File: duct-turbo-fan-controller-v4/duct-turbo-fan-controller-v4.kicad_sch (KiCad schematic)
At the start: 45 parts, among them J1 Screw_Terminal_01x04, J2 Conn_01x04, J3 USB_OTG, J4 AudioJack4, J7 Conn_01x04, Q1 MMBT3904, Q2 BSS84, SW1 SW_Push, SW2 SW_Push, U1 SCD41-D-R2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

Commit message: Reduce size of R8 to 0603. Improve labels of LEDs.
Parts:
- R8: footprint Resistor_SMD:R_0805_2012Metric_Pad1.20x1.40mm_HandSolder -> Resistor_SMD:R_0603_1608Metric_Pad0.98x0.95mm_HandSolder
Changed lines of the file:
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@@
 			)
 		)
-		(property "Footprint" "Resistor_SMD:R_0805_2012Metric_Pad1.20x1.40mm_HandSolder"
+		(property "Footprint" "Resistor_SMD:R_0603_1608Metric_Pad0.98x0.95mm_HandSolder"
 			(at 96.52 77.47 0)
 			(effects

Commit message: Add values to led resistors. Redraw zone fills.
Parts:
- D4: value LED_Small -> LED Green
- D5: value LED_Small -> LED Red
- R15, R16: value R_Small -> 1k
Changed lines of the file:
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@@
 			)
 		)
-		(property "Value" "R_Small"
+		(property "Value" "1k"
 			(at 243.84 27.9399 0)
 			(effects
@@
 			)
 		)
-		(property "Value" "LED_Small"
+		(property "Value" "LED Green"
 			(at 259.08 32.9564 90)
 			(effects
@@
 			)
 		)
-		(property "Value" "R_Small"
+		(property "Value" "1k"
 			(at 259.08 27.9399 0)
 			(effects
@@
 			)
 		)
-		(property "Value" "LED_Small"
+		(property "Value" "LED Red"
 			(at 243.84 32.9564 90)
 			(effects

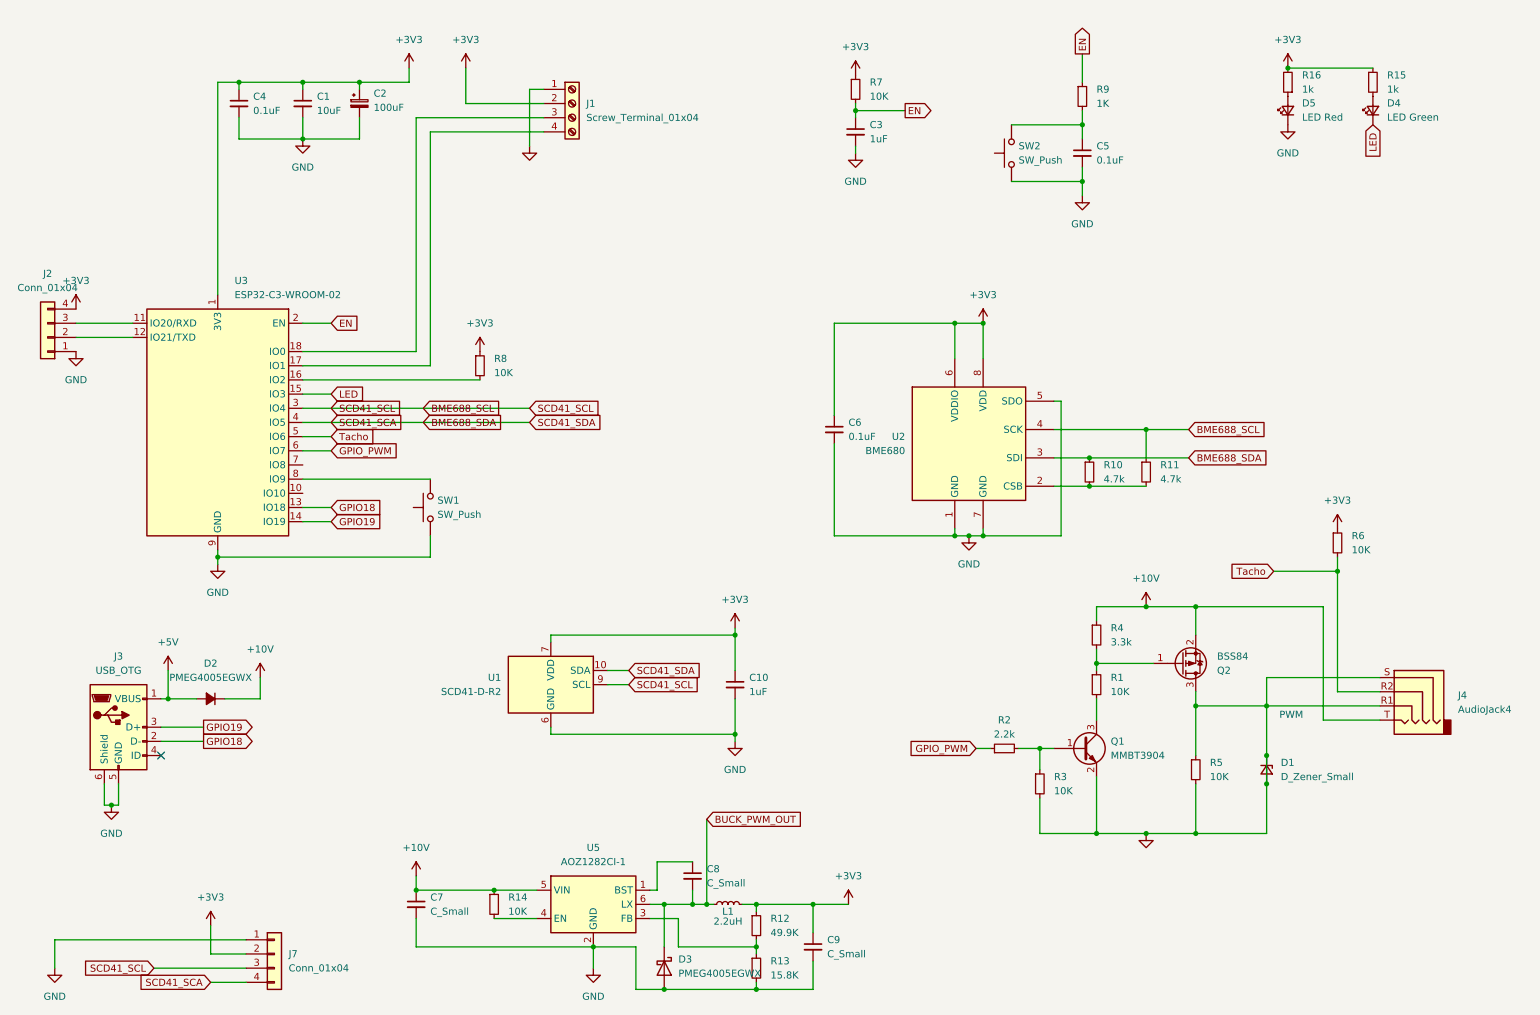
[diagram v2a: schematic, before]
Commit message: Fix a couple of schematic errors.
1. External PWM was tied to ground.
2. BME688 SCA and SCL pins were tied together.
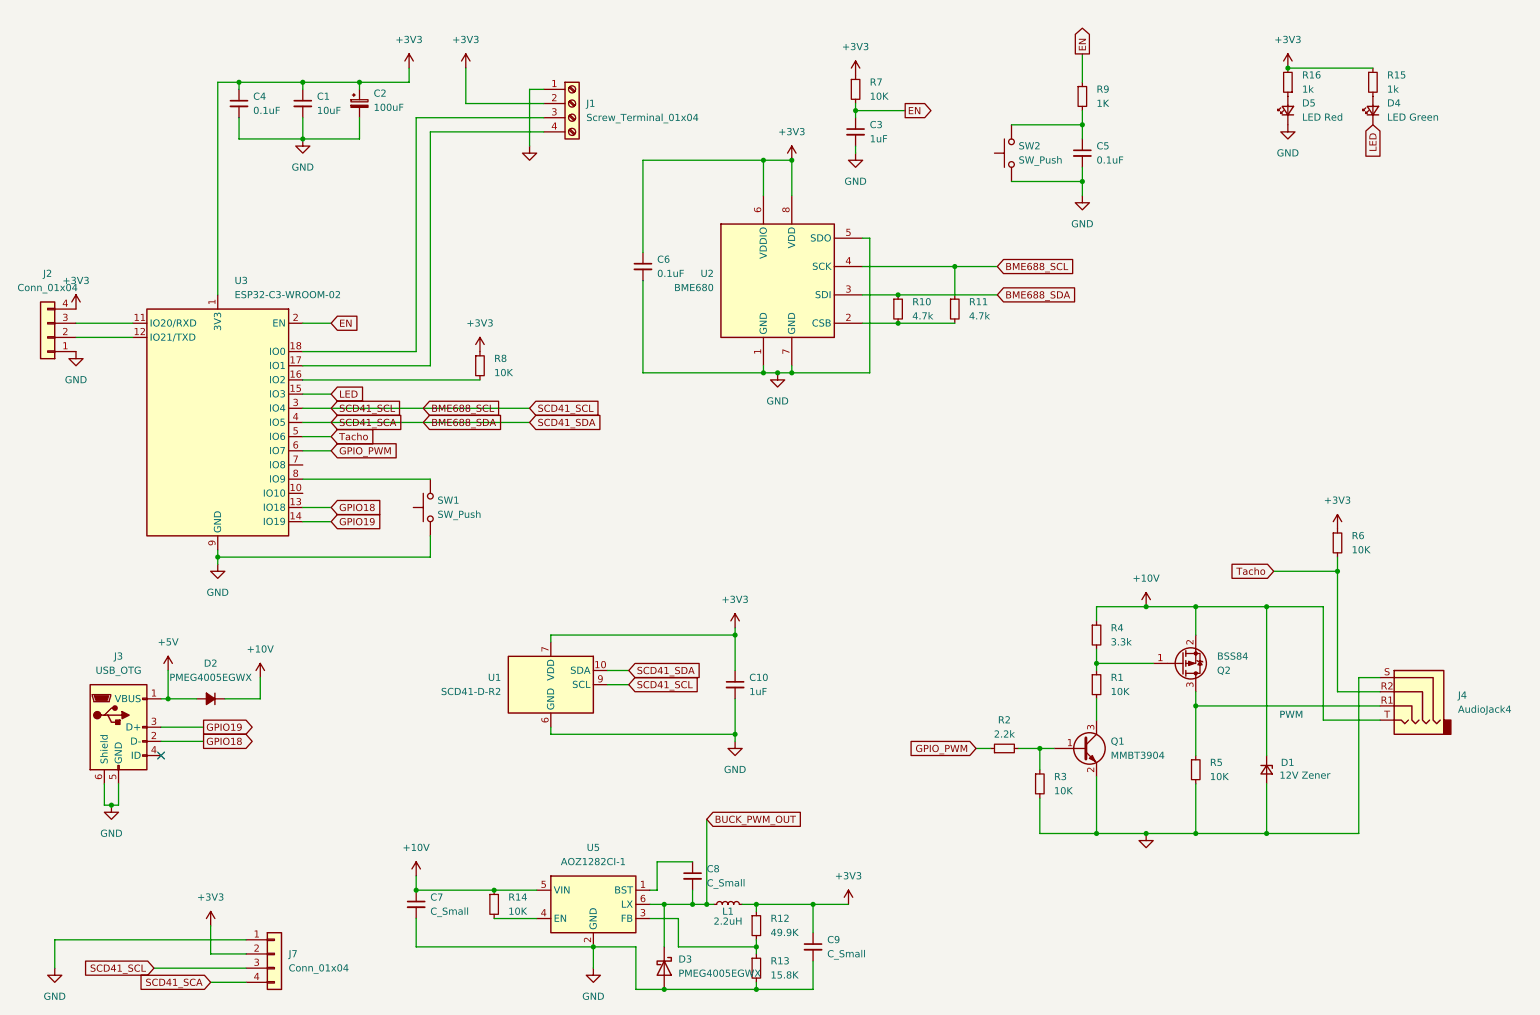
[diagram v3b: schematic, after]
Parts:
- D1: value D_Zener_Small -> 12V Zener
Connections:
- net +10V: now also D1.1 (K)
- net GND: no longer D1.1 (K), J4.R1, Q2.3 (D), R5.1
- new net: J4.R1, Q2.3 (D), R5.1
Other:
- moved on the sheet: C6, R10, R11, U2

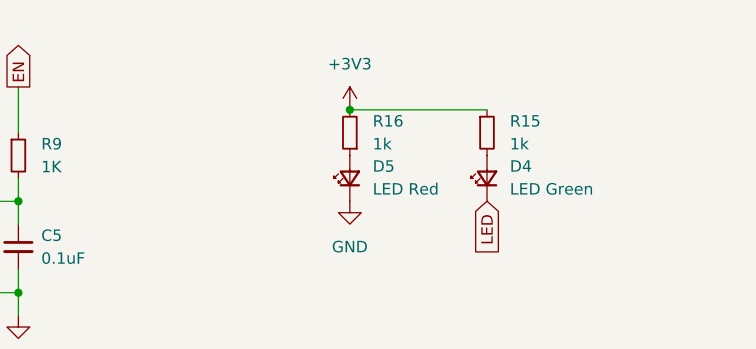
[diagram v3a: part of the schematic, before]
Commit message: Add gnd tracks where fill zone incomplete.
Update leds in schematic to be more readable.
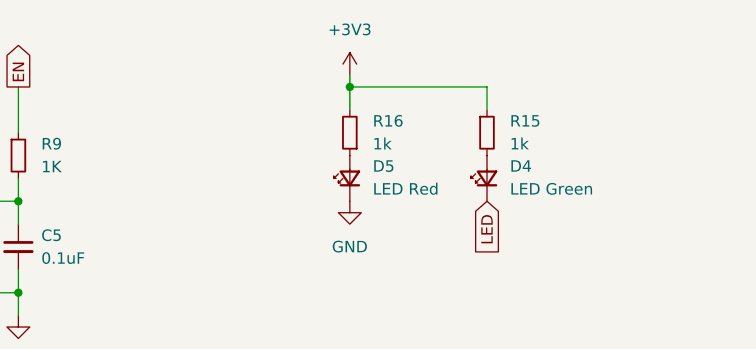
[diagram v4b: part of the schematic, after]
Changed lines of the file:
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@@
 	)
 	(junction
+		(at 241.3 21.59)
+		(diameter 0)
+		(color 0 0 0 0)
+	)
+	(junction
 		(at 207.01 161.29)
 		(diameter 0)
@@
 	)
 	(junction
-		(at 241.3 24.13)
-		(diameter 0)
-		(color 0 0 0 0)
-	)
-	(junction
 		(at 99.06 171.45)
 		(diameter 0)
@@
 	(wire
 		(pts
-			(xy 241.3 24.13) (xy 256.54 24.13)
+			(xy 241.3 21.59) (xy 256.54 21.59)
 		)
 		(stroke
@@
 	(wire
 		(pts
+			(xy 241.3 20.32) (xy 241.3 21.59)
+		)
+		(stroke
+			(width 0)
+			(type default)
+		)
+	)
+	(wire
+		(pts
 			(xy 237.49 120.65) (xy 237.49 147.32)
 		)
@@
 	(wire
 		(pts
+			(xy 256.54 21.59) (xy 256.54 24.13)
+		)
+		(stroke
+			(width 0)
+			(type default)
+		)
+	)
+	(wire
+		(pts
 			(xy 224.79 120.65) (xy 224.79 125.73)
 		)
@@
 	(wire
 		(pts
+			(xy 241.3 21.59) (xy 241.3 24.13)
+		)
+		(stroke
+			(width 0)
+			(type default)
+		)
+	)
+	(wire
+		(pts
 			(xy 29.21 156.21) (xy 30.48 156.21)
 		)
@@
 	(symbol
 		(lib_id "power:+3.3V")
-		(at 241.3 24.13 0)
+		(at 241.3 20.32 0)
 		(unit 1)
 		(exclude_from_sim no)
@@
 		(fields_autoplaced yes)
 		(property "Reference" "#PWR029"
-			(at 241.3 27.94 0)
+			(at 241.3 24.13 0)
 			(effects
 				(font
@@
 		)
 		(property "Value" "+3V3"
-			(at 241.3 19.05 0)
+			(at 241.3 15.24 0)
 			(effects
 				(font
@@
 		)
 		(property "Footprint" ""
-			(at 241.3 24.13 0)
+			(at 241.3 20.32 0)
 			(effects
 				(font
@@
 		)
 		(property "Datasheet" ""
-			(at 241.3 24.13 0)
+			(at 241.3 20.32 0)
 			(effects
 				(font
@@
 		)
 		(property "Description" ""
-			(at 241.3 24.13 0)
+			(at 241.3 20.32 0)
 			(effects
 				(font
